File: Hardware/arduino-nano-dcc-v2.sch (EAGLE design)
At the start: 43 parts, among them IC1 7805TV, IC3 MEGA328-P, Q2 TIP41C, X1 22-23-2031

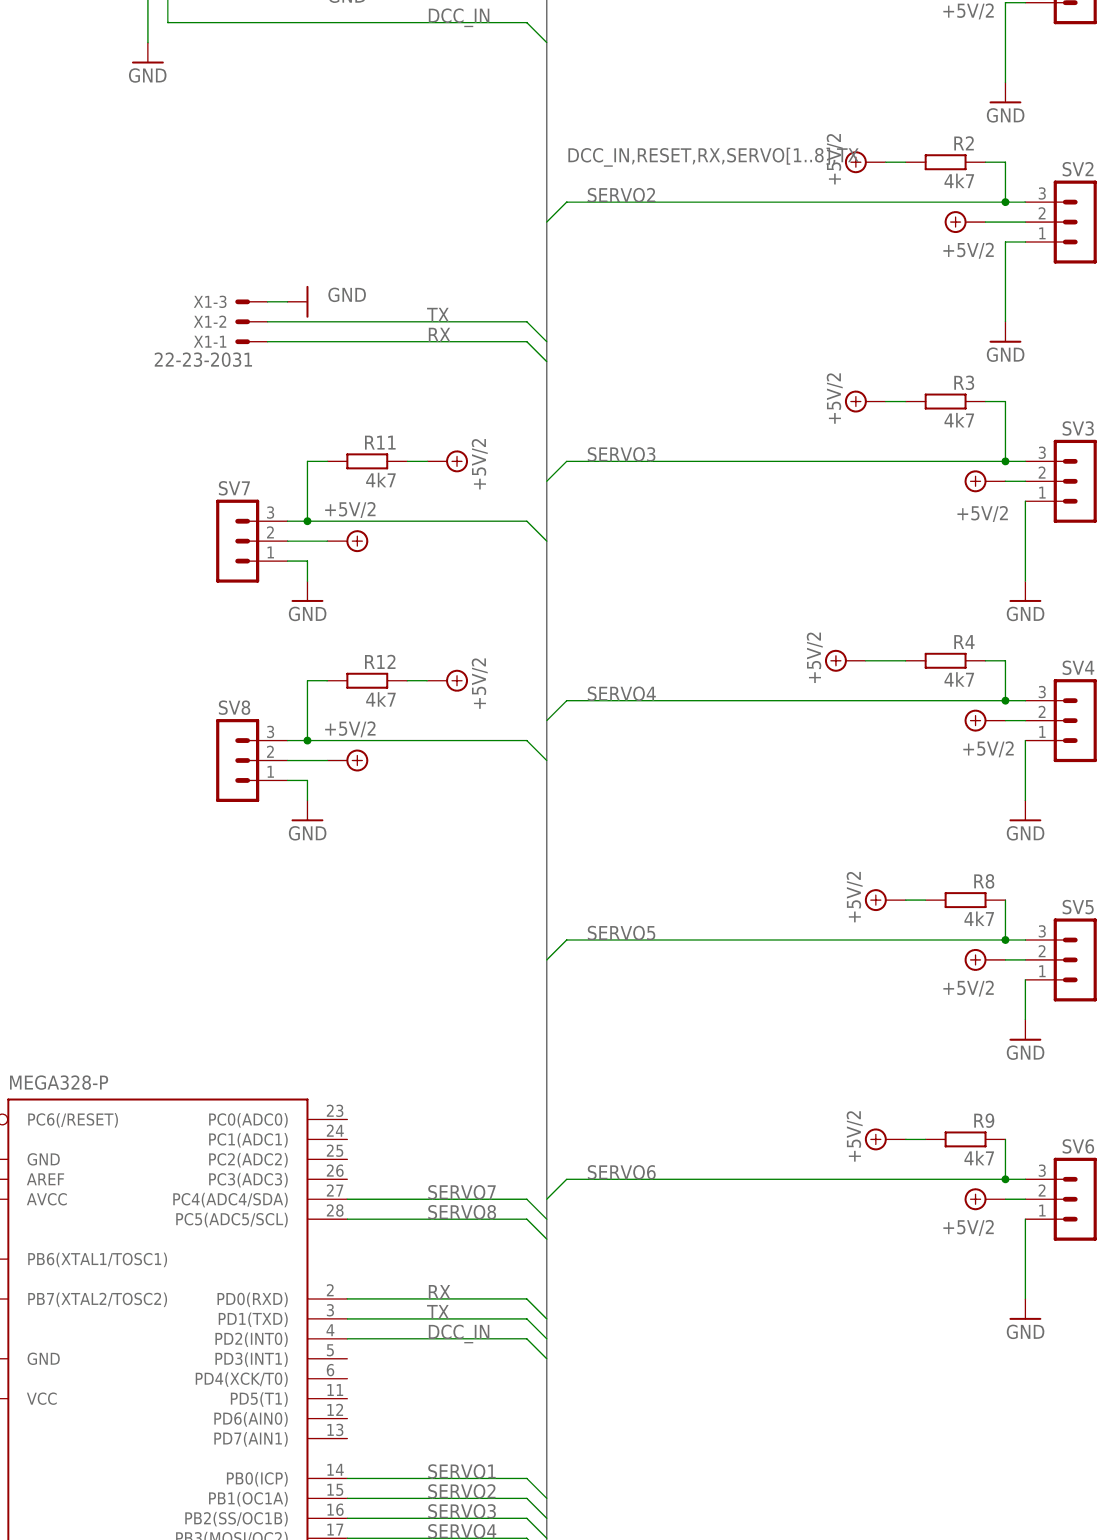
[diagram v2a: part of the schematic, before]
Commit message: Added led and added zipfile for pcb production at JclPcb.
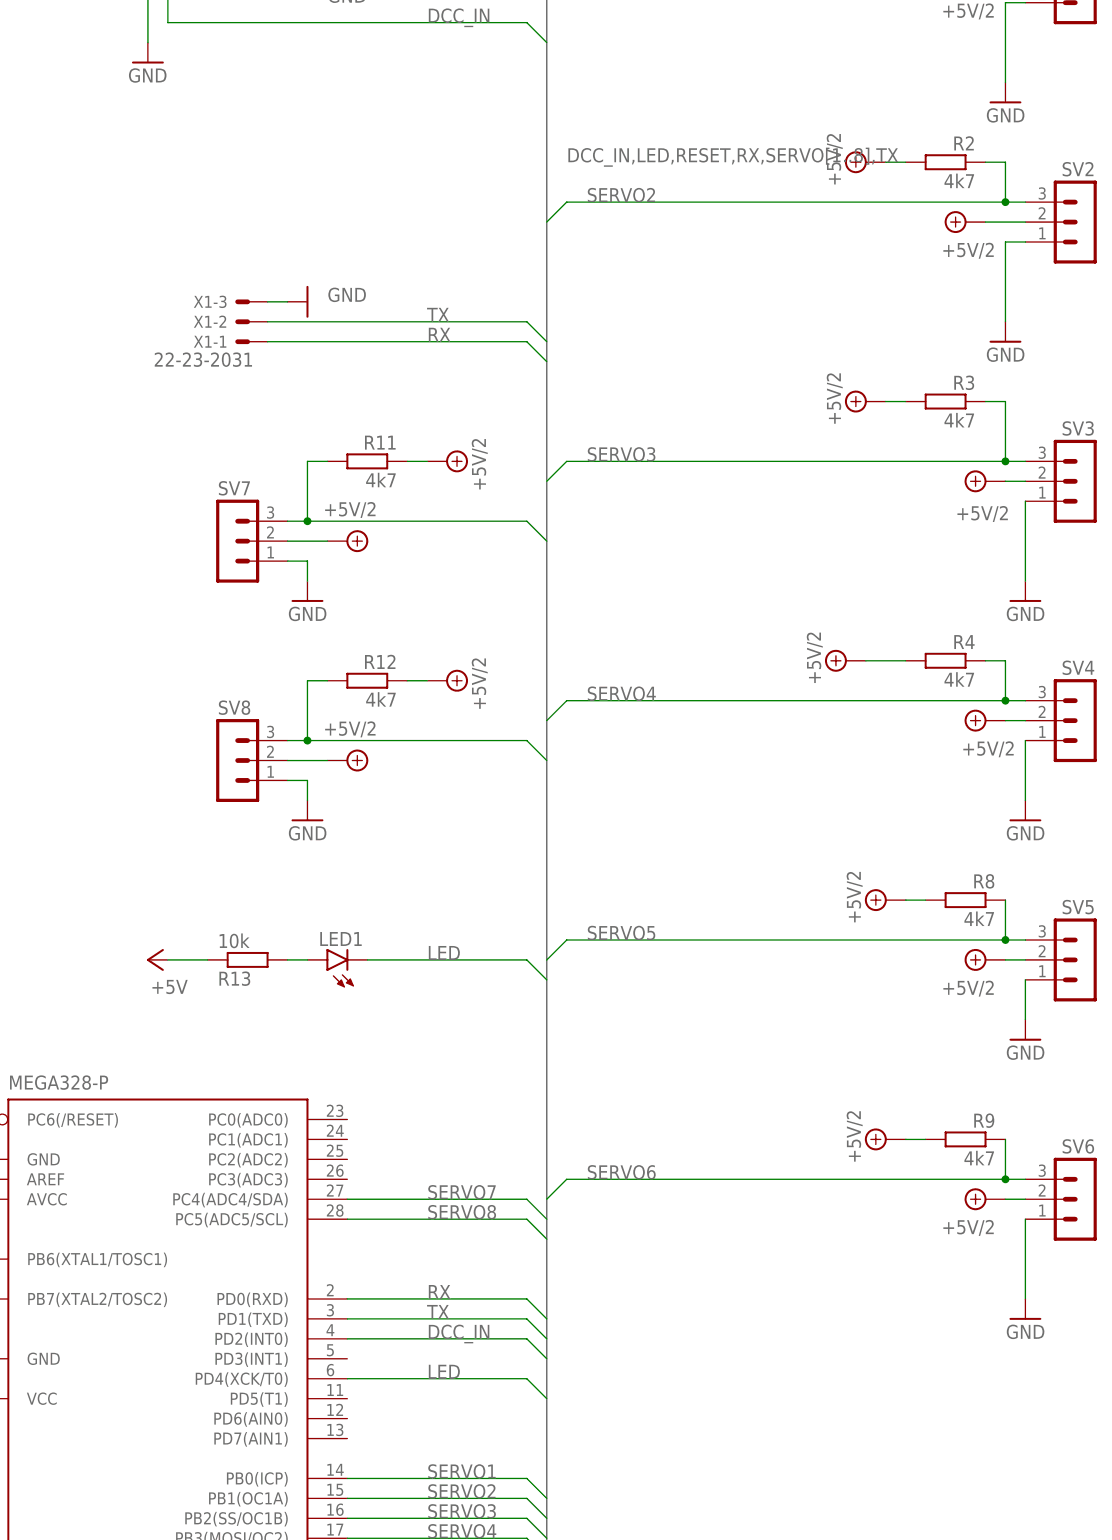
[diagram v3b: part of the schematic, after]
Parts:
- added LED1: (no value), led:LED3MM
- added R13: 10k, rcl:R-EU_0204/2V
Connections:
- new net LED: IC3.PD4(XCK/T0), LED1.C
- new net N$7: LED1.A, R13.2
- net +5V: now also R13.1
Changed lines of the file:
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@@
 <part name="SUPPLY17" library="supply2" library_urn="urn:adsk.eagle:library:372" deviceset="+5V/2" device=""/>
 <part name="R12" library="rcl" deviceset="R-EU_" device="0204/5" value="4k7"/>
+<part name="LED1" library="led" library_urn="urn:adsk.eagle:library:259" deviceset="LED" device="3MM" package3d_urn="urn:adsk.eagle:package:15797/1"/>
+<part name="P+2" library="supply1" library_urn="urn:adsk.eagle:library:371" deviceset="+5V" device=""/>
+<part name="R13" library="rcl" deviceset="R-EU_" device="0204/2V" value="10k"/>
 </parts>
 <sheets>
@@
 <attribute name="VALUE" x="240.03" y="136.398" size="1.778" layer="96" rot="MR0"/>
 </instance>
+<instance part="LED1" gate="G$1" x="231.14" y="104.14" smashed="yes" rot="R90">
+<attribute name="NAME" x="235.712" y="107.696" size="1.778" layer="95" rot="R180"/>
+<attribute name="VALUE" x="235.712" y="109.855" size="1.778" layer="96" rot="R180"/>
+</instance>
+<instance part="P+2" gate="1" x="208.28" y="104.14" smashed="yes" rot="R90">
+<attribute name="VALUE" x="213.36" y="101.6" size="1.778" layer="96" rot="R180"/>
+</instance>
+<instance part="R13" gate="G$1" x="220.98" y="104.14" smashed="yes" rot="MR180">
+<attribute name="NAME" x="217.17" y="102.6414" size="1.778" layer="95" rot="MR180"/>
+<attribute name="VALUE" x="217.17" y="107.442" size="1.778" layer="96" rot="MR180"/>
+</instance>
 </instances>
 <busses>
-<bus name="DCC_IN,RESET,RX,SERVO[1..8],TX">
+<bus name="DCC_IN,LED,RESET,RX,SERVO[1..8],TX">
 <segment>
 <wire x1="259.08" y1="243.84" x2="259.08" y2="17.78" width="0.762" layer="92"/>
@@
 <wire x1="182.88" y1="48.26" x2="185.42" y2="48.26" width="0.1524" layer="91"/>
 </segment>
+<segment>
+<pinref part="R13" gate="G$1" pin="1"/>
+<pinref part="P+2" gate="1" pin="+5V"/>
+<wire x1="210.82" y1="104.14" x2="215.9" y2="104.14" width="0.1524" layer="91"/>
+</segment>
 </net>
 <net name="GND" class="0">
@@
 </segment>
 </net>
+<net name="LED" class="0">
+<segment>
+<wire x1="259.08" y1="101.6" x2="256.54" y2="104.14" width="0.1524" layer="91"/>
+<pinref part="LED1" gate="G$1" pin="C"/>
+<wire x1="256.54" y1="104.14" x2="236.22" y2="104.14" width="0.1524" layer="91"/>
+<label x="243.84" y="104.14" size="1.778" layer="95"/>
+</segment>
+<segment>
+<wire x1="259.08" y1="48.26" x2="256.54" y2="50.8" width="0.1524" layer="91"/>
+<pinref part="IC3" gate="G$1" pin="PD4(XCK/T0)"/>
+<wire x1="256.54" y1="50.8" x2="233.68" y2="50.8" width="0.1524" layer="91"/>
+<label x="243.84" y="50.8" size="1.778" layer="95"/>
+</segment>
+</net>
+<net name="N$7" class="0">
+<segment>
+<pinref part="LED1" gate="G$1" pin="A"/>
+<pinref part="R13" gate="G$1" pin="2"/>
+<wire x1="226.06" y1="104.14" x2="228.6" y2="104.14" width="0.1524" layer="91"/>
+</segment>
+</net>

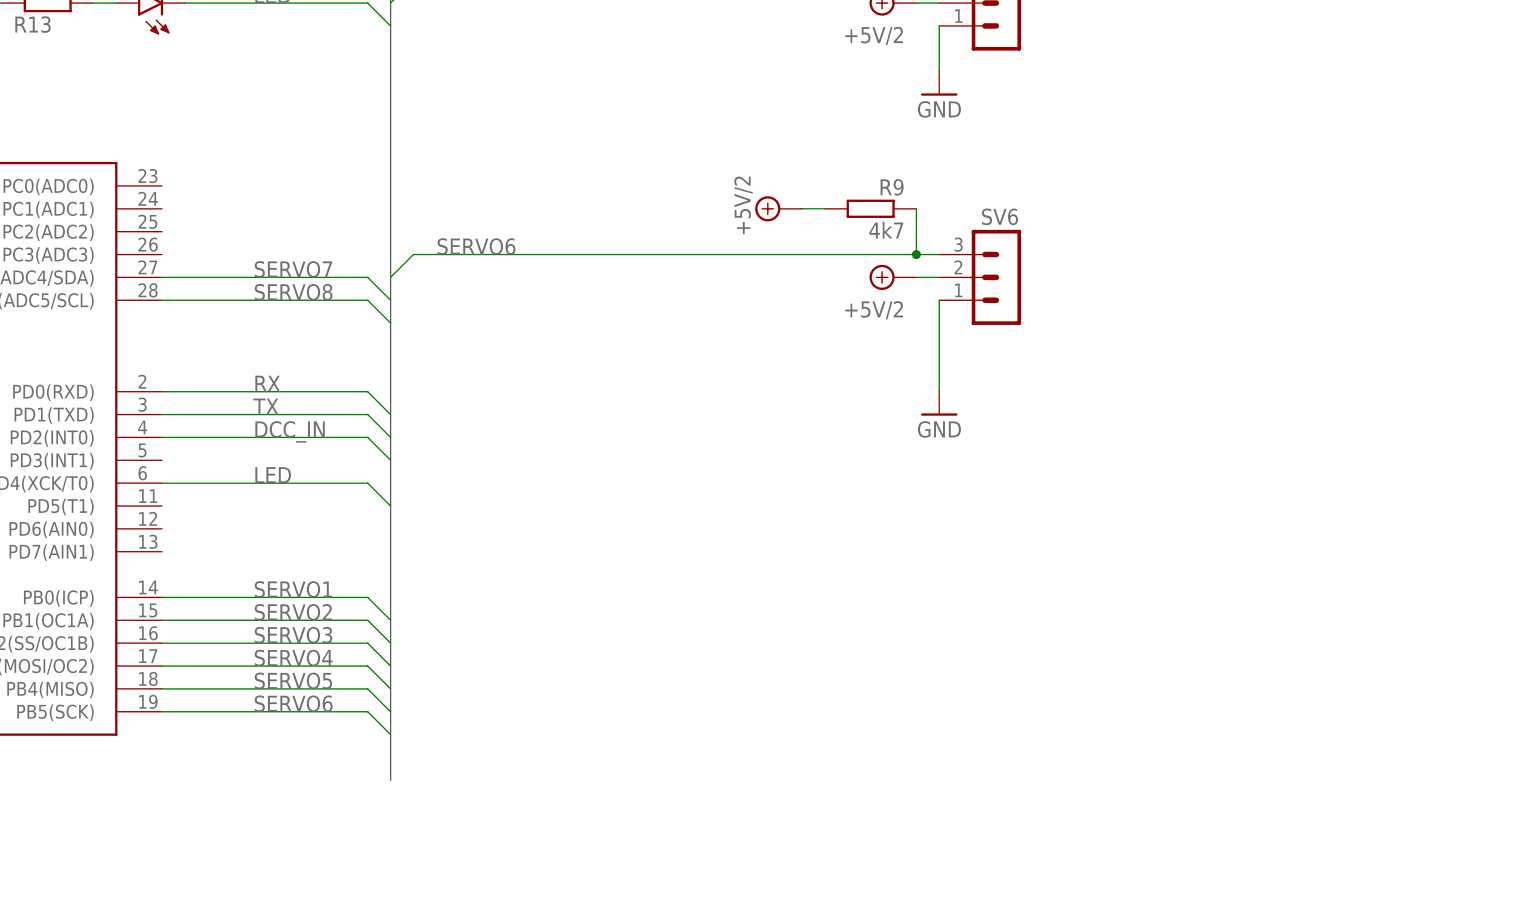
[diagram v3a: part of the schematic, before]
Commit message: * Pin PB5 does not work, so moved to PC0.  * Run led added.
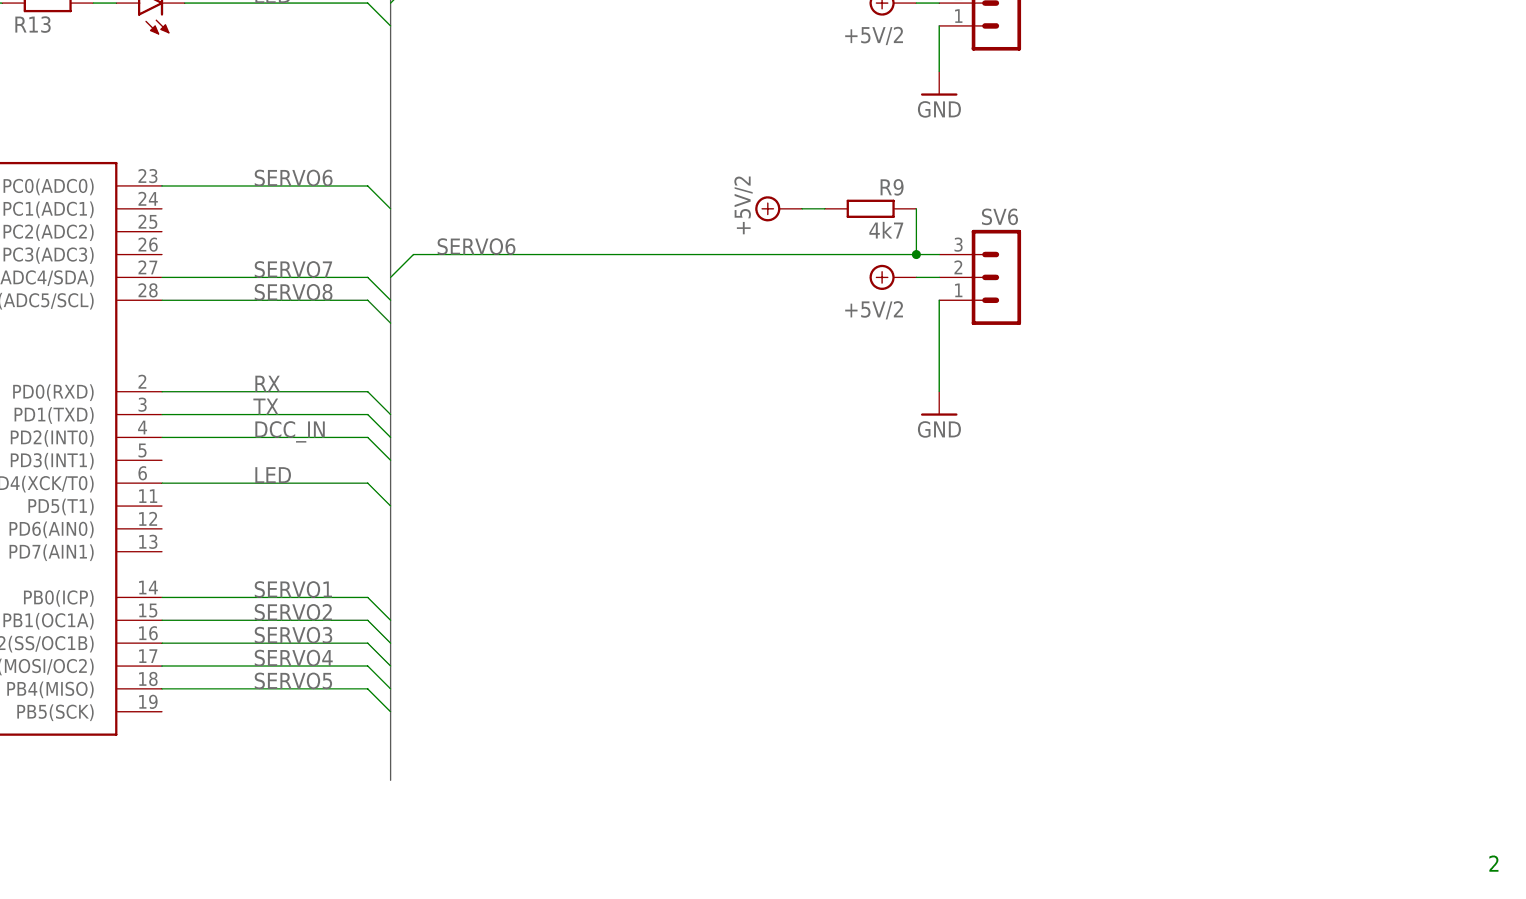
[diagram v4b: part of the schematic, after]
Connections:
- net SERVO6: now also IC3.PC0(ADC0); no longer IC3.PB5(SCK)
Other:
- note added: "2"
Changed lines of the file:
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@@
 <grid distance="0.1" unitdist="inch" unit="inch" style="lines" multiple="1" display="no" altdistance="0.01" altunitdist="inch" altunit="inch"/>
 <layers>
-<layer number="1" name="Top" color="4" fill="1" visible="yes" active="no"/>
-<layer number="16" name="Bottom" color="1" fill="1" visible="yes" active="no"/>
-<layer number="17" name="Pads" color="2" fill="1" visible="yes" active="no"/>
-<layer number="18" name="Vias" color="2" fill="1" visible="yes" active="no"/>
-<layer number="19" name="Unrouted" color="6" fill="1" visible="yes" active="no"/>
-<layer number="20" name="Dimension" color="24" fill="1" visible="yes" active="no"/>
-<layer number="21" name="tPlace" color="7" fill="1" visible="yes" active="no"/>
-<layer number="22" name="bPlace" color="7" fill="1" visible="yes" active="no"/>
-<layer number="23" name="tOrigins" color="15" fill="1" visible="yes" active="no"/>
-<layer number="24" name="bOrigins" color="15" fill="1" visible="yes" active="no"/>
-<layer number="25" name="tNames" color="7" fill="1" visible="yes" active="no"/>
-<layer number="26" name="bNames" color="7" fill="1" visible="yes" active="no"/>
-<layer number="27" name="tValues" color="7" fill="1" visible="yes" active="no"/>
-<layer number="28" name="bValues" color="7" fill="1" visible="yes" active="no"/>
+<layer number="1" name="Top" color="4" fill="1" visible="no" active="no"/>
+<layer number="16" name="Bottom" color="1" fill="1" visible="no" active="no"/>
+<layer number="17" name="Pads" color="2" fill="1" visible="no" active="no"/>
+<layer number="18" name="Vias" color="2" fill="1" visible="no" active="no"/>
+<layer number="19" name="Unrouted" color="6" fill="1" visible="no" active="no"/>
+<layer number="20" name="Dimension" color="24" fill="1" visible="no" active="no"/>
+<layer number="21" name="tPlace" color="7" fill="1" visible="no" active="no"/>
+<layer number="22" name="bPlace" color="7" fill="1" visible="no" active="no"/>
+<layer number="23" name="tOrigins" color="15" fill="1" visible="no" active="no"/>
+<layer number="24" name="bOrigins" color="15" fill="1" visible="no" active="no"/>
+<layer number="25" name="tNames" color="7" fill="1" visible="no" active="no"/>
+<layer number="26" name="bNames" color="7" fill="1" visible="no" active="no"/>
+<layer number="27" name="tValues" color="7" fill="1" visible="no" active="no"/>
+<layer number="28" name="bValues" color="7" fill="1" visible="no" active="no"/>
 <layer number="29" name="tStop" color="7" fill="3" visible="no" active="no"/>
 <layer number="30" name="bStop" color="7" fill="6" visible="no" active="no"/>
@@
 <layer number="35" name="tGlue" color="7" fill="4" visible="no" active="no"/>
 <layer number="36" name="bGlue" color="7" fill="5" visible="no" active="no"/>
-<layer number="37" name="tTest" color="7" fill="1" visible="yes" active="no"/>
-<layer number="38" name="bTest" color="7" fill="1" visible="yes" active="no"/>
+<layer number="37" name="tTest" color="7" fill="1" visible="no" active="no"/>
+<layer number="38" name="bTest" color="7" fill="1" visible="no" active="no"/>
 <layer number="39" name="tKeepout" color="4" fill="11" visible="no" active="no"/>
 <layer number="40" name="bKeepout" color="1" fill="11" visible="no" active="no"/>
@@
 <layer number="44" name="Drills" color="7" fill="1" visible="no" active="no"/>
 <layer number="45" name="Holes" color="7" fill="1" visible="no" active="no"/>
-<layer number="46" name="Milling" color="3" fill="1" visible="yes" active="no"/>
-<layer number="47" name="Measures" color="7" fill="1" visible="yes" active="no"/>
-<layer number="48" name="Document" color="7" fill="1" visible="yes" active="no"/>
-<layer number="49" name="Reference" color="7" fill="1" visible="yes" active="no"/>
-<layer number="51" name="tDocu" color="7" fill="1" visible="yes" active="no"/>
-<layer number="52" name="bDocu" color="7" fill="1" visible="yes" active="no"/>
+<layer number="46" name="Milling" color="3" fill="1" visible="no" active="no"/>
+<layer number="47" name="Measures" color="7" fill="1" visible="no" active="no"/>
+<layer number="48" name="Document" color="7" fill="1" visible="no" active="no"/>
+<layer number="49" name="Reference" color="7" fill="1" visible="no" active="no"/>
+<layer number="51" name="tDocu" color="7" fill="1" visible="no" active="no"/>
+<layer number="52" name="bDocu" color="7" fill="1" visible="no" active="no"/>
 <layer number="88" name="SimResults" color="9" fill="1" visible="yes" active="yes"/>
 <layer number="89" name="SimProbes" color="9" fill="1" visible="yes" active="yes"/>
@@
 <sheet>
 <plain>
+<text x="381" y="7.62" size="1.778" layer="91">2</text>
 </plain>
 <instances>
@@
 </segment>
 <segment>
-<wire x1="259.08" y1="22.86" x2="256.54" y2="25.4" width="0.1524" layer="91"/>
-<pinref part="IC3" gate="G$1" pin="PB5(SCK)"/>
-<wire x1="256.54" y1="25.4" x2="233.68" y2="25.4" width="0.1524" layer="91"/>
-<label x="243.84" y="25.4" size="1.778" layer="95"/>
-</segment>
-</net>
+<wire x1="259.08" y1="81.28" x2="256.54" y2="83.82" width="0.1524" layer="91"/>
+<pinref part="IC3" gate="G$1" pin="PC0(ADC0)"/>
+<wire x1="256.54" y1="83.82" x2="233.68" y2="83.82" width="0.1524" layer="91"/>
+<label x="243.84" y="83.82" size="1.778" layer="95"/>
+</segment>
+</net>
